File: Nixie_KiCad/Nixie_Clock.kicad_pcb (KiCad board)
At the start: 2 copper layers, 140 x 60 mm, 39 parts, among them U1 K155ID1, U10 K155ID1, U11 IN-14, U12 K155ID1, U13 IN-14, U14 DS3231, U2 IN-14, U3 K155ID1, U4 IN-14, U5 K155ID1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

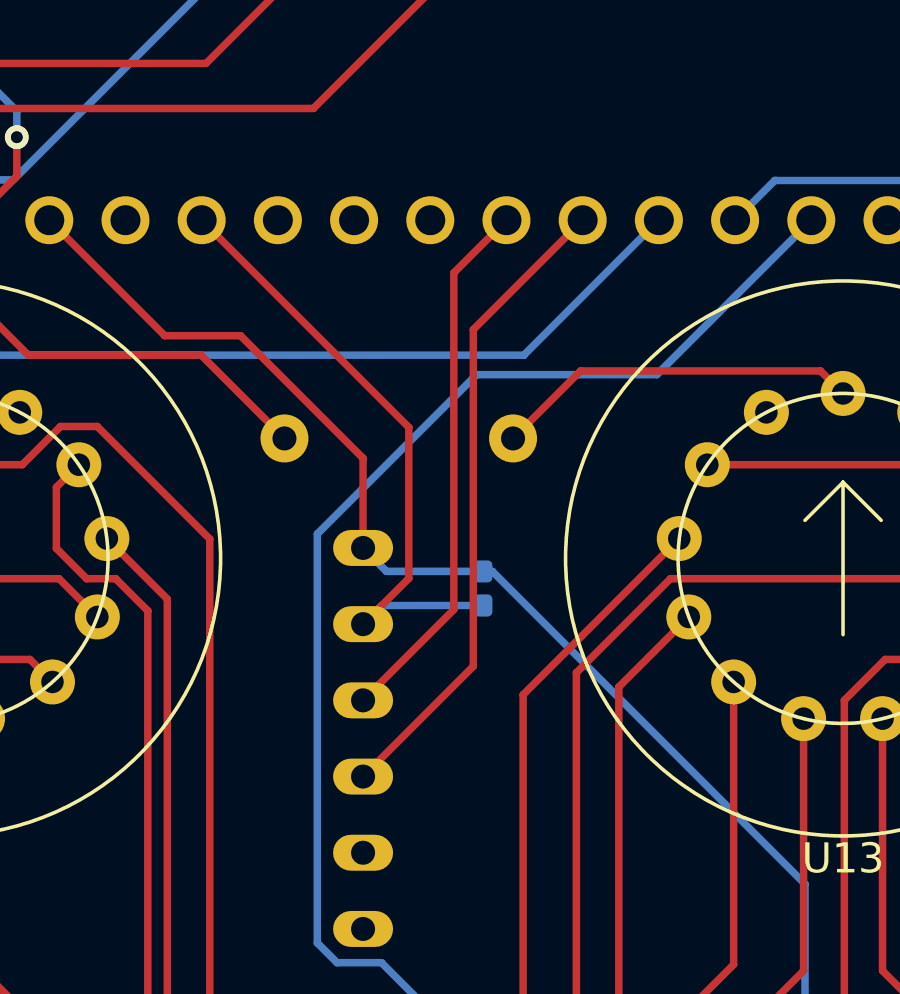
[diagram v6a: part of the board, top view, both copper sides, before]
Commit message: Corrected RTC pinout
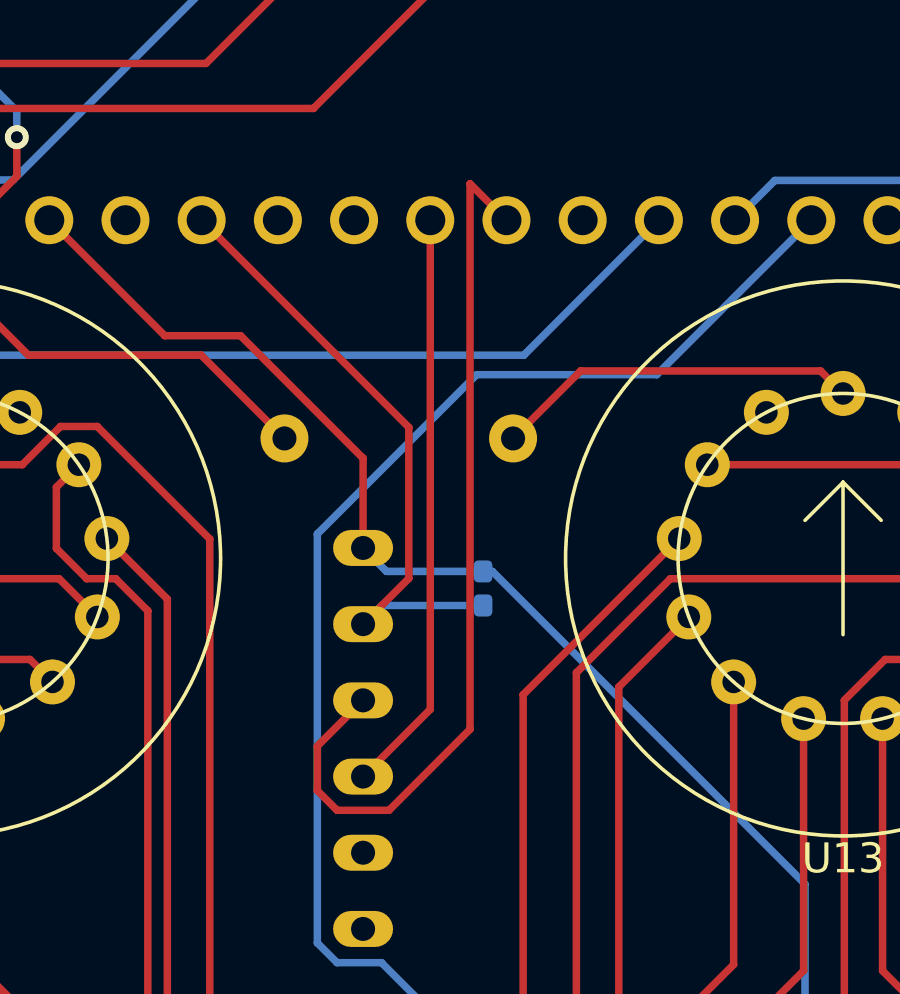
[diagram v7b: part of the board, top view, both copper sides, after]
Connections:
- A1 pad 22: SCL -> Net-(A1-Pad22)
- A1 pad 24: Net-(A1-Pad24) -> SCL
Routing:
- net SDA: track 18.0 -> 30.0 mm
- net SCL: track 21.6 -> 19.5 mm
